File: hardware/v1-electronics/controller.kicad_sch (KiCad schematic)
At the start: 41 parts, among them IC1 IS31FL3733-QFLS4-TR, IC2 IS31FL3733-QFLS4-TR, IC3 IS31FL3741A-QFLS4-TR, U1 MDBT50Q-1MV2

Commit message: feat(v1 hardware): RGBW LED matrix halve 1
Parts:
- removed C27, C28, C29, C30, C31, C32, C34: C_Small, symbol Device:C_Small
- removed IC3: IS31FL3741A-QFLS4-TR, QFN40P700X700X80-61N-D, symbol Lumissil Microsystems:IS31FL3741A-QFLS4-TR
- removed R41, R42, R67: R_Small, symbol Device:R_Small
- added R148, R149, R150, R151, R152, R153, R154, R155, R156, R157, R158, R159, R160, R161, R162, R163, R164, R165, R166, R167, R168, R169, R170, R171, R172, R173, R174, R175, R176, R43, R44, R68: R_Small, symbol Device:R_Small
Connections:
- net GND: now also IC1.49 (EP), IC2.49 (EP)
- net I2C1_SCL: now also IC2.42 (SCL)
- net I2C1_SDA: now also IC2.41 (SDA); no longer IC2.45 (INTB), R115.2
- net SDB2: now also IC2.46 (SDB); no longer IC1.40 (SYNC), IC2.40 (SYNC)
- net ISET1 renamed R_EXT1
- net ISET2 renamed R_EXT2
- new net CS10_G_1: R163.1
- new net CS10_G_2: R164.1
- new net CS11_R_1: R165.1
- new net CS11_R_2: R166.1
- new net CS12_W_1: R167.1
- new net CS12_W_2: R168.1
- new net CS13_B_1: R169.1
- new net CS13_B_2: R170.1
- new net CS14_G_1: R171.1
- new net CS14_G_2: R172.1
- new net CS15_R_1: R173.1
- new net CS15_R_2: R174.1
- new net CS16_W_1: R175.1
- new net CS16_W_2: R176.1
- new net CS1_B_1: R43.1
- new net CS1_B_2: R148.1
- new net CS2_G_1: R44.1
- new net CS2_G_2: R149.1
- new net CS3_R_1: R68.1
- new net CS3_R_2: R150.1
- new net CS4_W_1: R151.1
- new net CS4_W_2: R152.1
- new net CS5_B_1: R153.1
- new net CS5_B_2: R154.1
- new net CS6_G_1: R155.1
- new net CS6_G_2: R156.1
- new net CS7_R_1: R157.1
- new net CS7_R_2: R158.1
- new net CS8_W_1: R159.1
- new net CS8_W_2: R160.1
- new net CS9_B_1: R161.1
- new net CS9_B_2: R162.1
- new net INTB2: IC2.45 (INTB), R115.2
- new net SYNC: IC1.40 (SYNC), IC2.40 (SYNC)
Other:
- note removed: "Some thought needs to be done as to what V_IO/MCU should be"
- moved on the sheet: C21, C22, C23, C24, C25, C26, C33, C35, C36, C37, C38, C39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

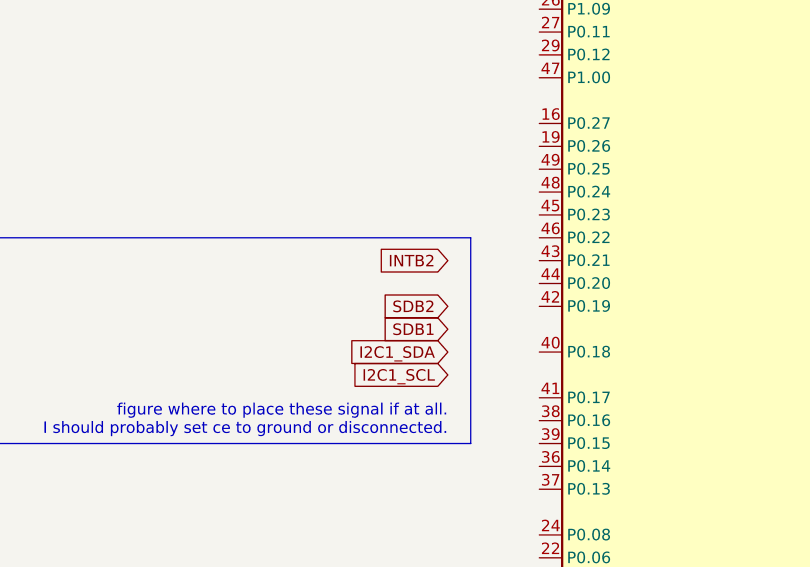
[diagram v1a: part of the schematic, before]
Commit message: feat(v1 hardware):second half of LED Matrix
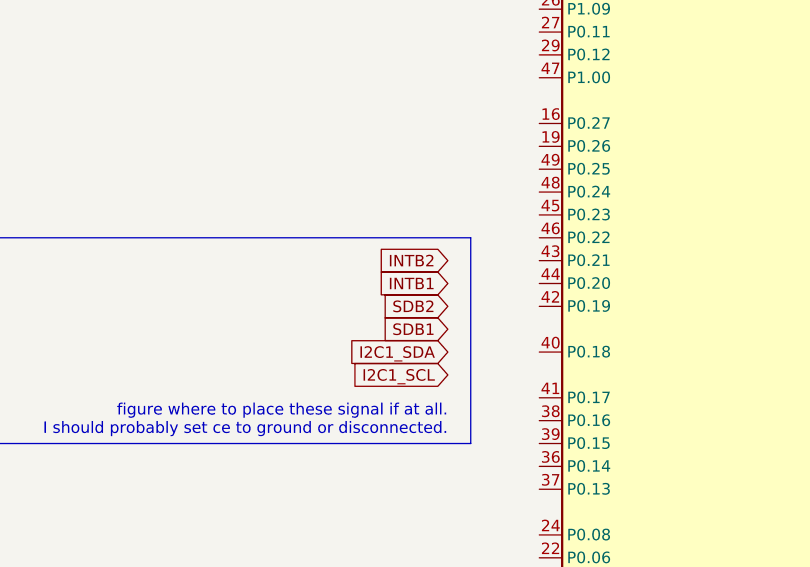
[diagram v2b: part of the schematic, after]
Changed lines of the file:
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@@
+		)
+	)
+	(global_label "INTB1"
+		(shape input)
+		(at 317.5 66.04 180)
+		(fields_autoplaced yes)
+		(effects
+			(font
+				(size 1.27 1.27)
+			)
+			(justify right)
+		)
+		(property "Intersheetrefs" "${INTERSHEET_REFS}"
+			(at 309.1324 66.04 0)
+			(hide yes)
+			(show_name no)
+			(do_not_autoplace no)
+			(effects
+				(font
+					(size 1.27 1.27)
+				)
+				(justify right)
+			)
 		)
 	)

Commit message: feat(v1 hardware): clean up led matrix
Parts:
- removed R148, R149, R150, R151, R152, R153, R154, R155, R156, R157, R158, R159, R160, R161, R162, R163, R164, R165, R166, R167, R168, R169, R170, R171, R172, R173, R174, R175, R176, R43, R44, R68: R_Small, symbol Device:R_Small
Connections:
- net CS10_G_1: now also IC1.26 (CS10)
- net CS10_G_2: now also IC2.26 (CS10)
- net CS11_R_1: now also IC1.27 (CS11)
- net CS11_R_2: now also IC2.27 (CS11)
- net CS12_W_1: now also IC1.28 (CS12)
- net CS12_W_2: now also IC2.28 (CS12)
- net CS13_B_1: now also IC1.30 (CS13)
- net CS13_B_2: now also IC2.30 (CS13)
- net CS14_G_1: now also IC1.31 (CS14)
- net CS14_G_2: now also IC2.31 (CS14)
- net CS15_R_1: now also IC1.32 (CS15)
- net CS15_R_2: now also IC2.32 (CS15)
- net CS16_W_1: now also IC1.33 (CS16)
- net CS16_W_2: now also IC2.33 (CS16)
- net CS1_B_1: now also IC1.16 (CS1)
- net CS1_B_2: now also IC2.16 (CS1)
- net CS2_G_1: now also IC1.17 (CS2)
- net CS2_G_2: now also IC2.17 (CS2)
- net CS3_R_1: now also IC1.18 (CS3)
- net CS3_R_2: now also IC2.18 (CS3)
- net CS4_W_1: now also IC1.19 (CS4)
- net CS4_W_2: now also IC2.19 (CS4)
- net CS5_B_1: now also IC1.21 (CS5)
- net CS5_B_2: now also IC2.21 (CS5)
- net CS6_G_1: now also IC1.22 (CS6)
- net CS6_G_2: now also IC2.22 (CS6)
- net CS7_R_1: now also IC1.23 (CS7)
- net CS7_R_2: now also IC2.23 (CS7)
- net CS8_W_1: now also IC1.24 (CS8)
- net CS8_W_2: now also IC2.24 (CS8)
- net CS9_B_1: now also IC1.25 (CS9)
- net CS9_B_2: now also IC2.25 (CS9)
- net SW10_1: now also IC1.13 (SW10)
- net SW10_2: now also IC2.13 (SW10)
- net SW11_1: now also IC1.14 (SW11)
- net SW11_2: now also IC2.14 (SW11)
- net SW12_1: now also IC1.15 (SW12)
- net SW12_2: now also IC2.15 (SW12)
- net SW1_1: now also IC1.2 (SW1)
- net SW1_2: now also IC2.2 (SW1)
- net SW2_1: now also IC1.3 (SW2)
- net SW2_2: now also IC2.3 (SW2)
- net SW3_1: now also IC1.4 (SW3)
- net SW3_2: now also IC2.4 (SW3)
- net SW4_1: now also IC1.6 (SW4)
- net SW4_2: now also IC2.6 (SW4)
- net SW5_1: now also IC1.7 (SW5)
- net SW5_2: now also IC2.7 (SW5)
- net SW6_1: now also IC1.8 (SW6)
- net SW6_2: now also IC2.8 (SW6)
- net SW7_1: now also IC1.9 (SW7)
- net SW7_2: now also IC2.9 (SW7)
- net SW8_1: now also IC1.10 (SW8)
- net SW8_2: now also IC2.10 (SW8)
- net SW9_1: now also IC1.11 (SW9)
- net SW9_2: now also IC2.11 (SW9)
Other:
- note added: "LED Matric IC 1"
- note added: "LED Matric IC 2"
- moved on the sheet: C24, C25, C26, C33, C35, C36, C37, C38, C39, C40, C41, C42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

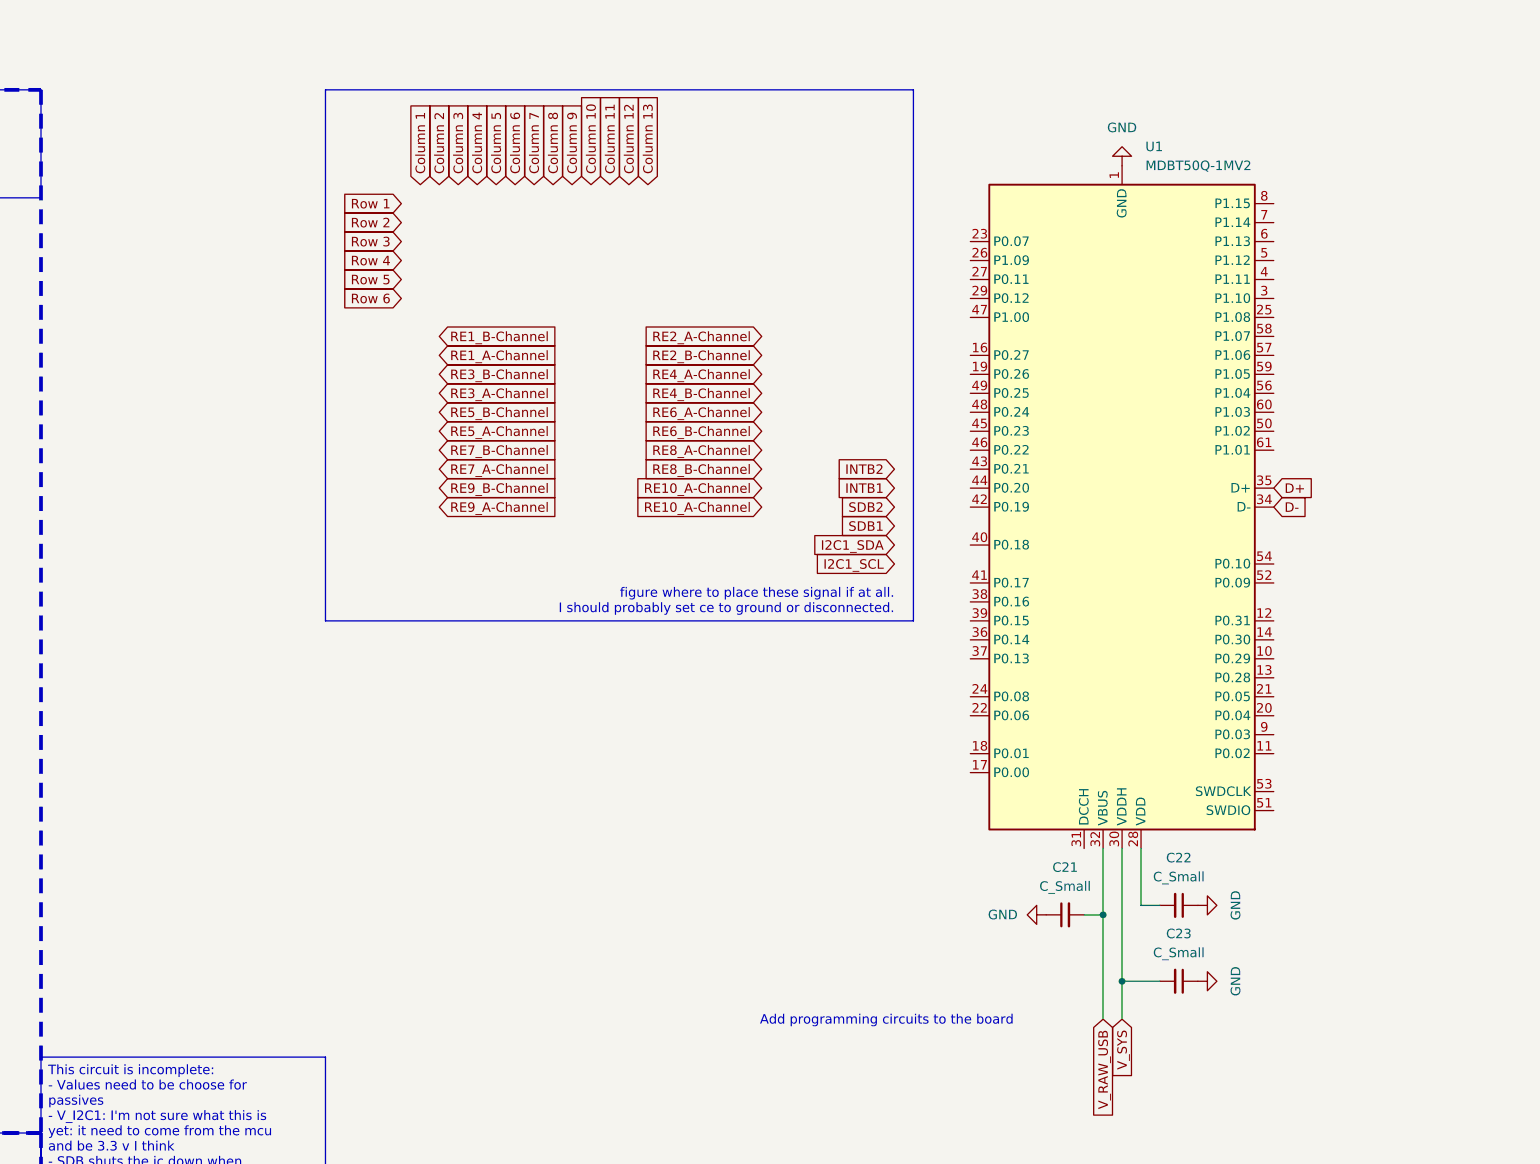
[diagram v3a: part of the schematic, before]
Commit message: feat(v1 hardware): start assigning pins on th mcu
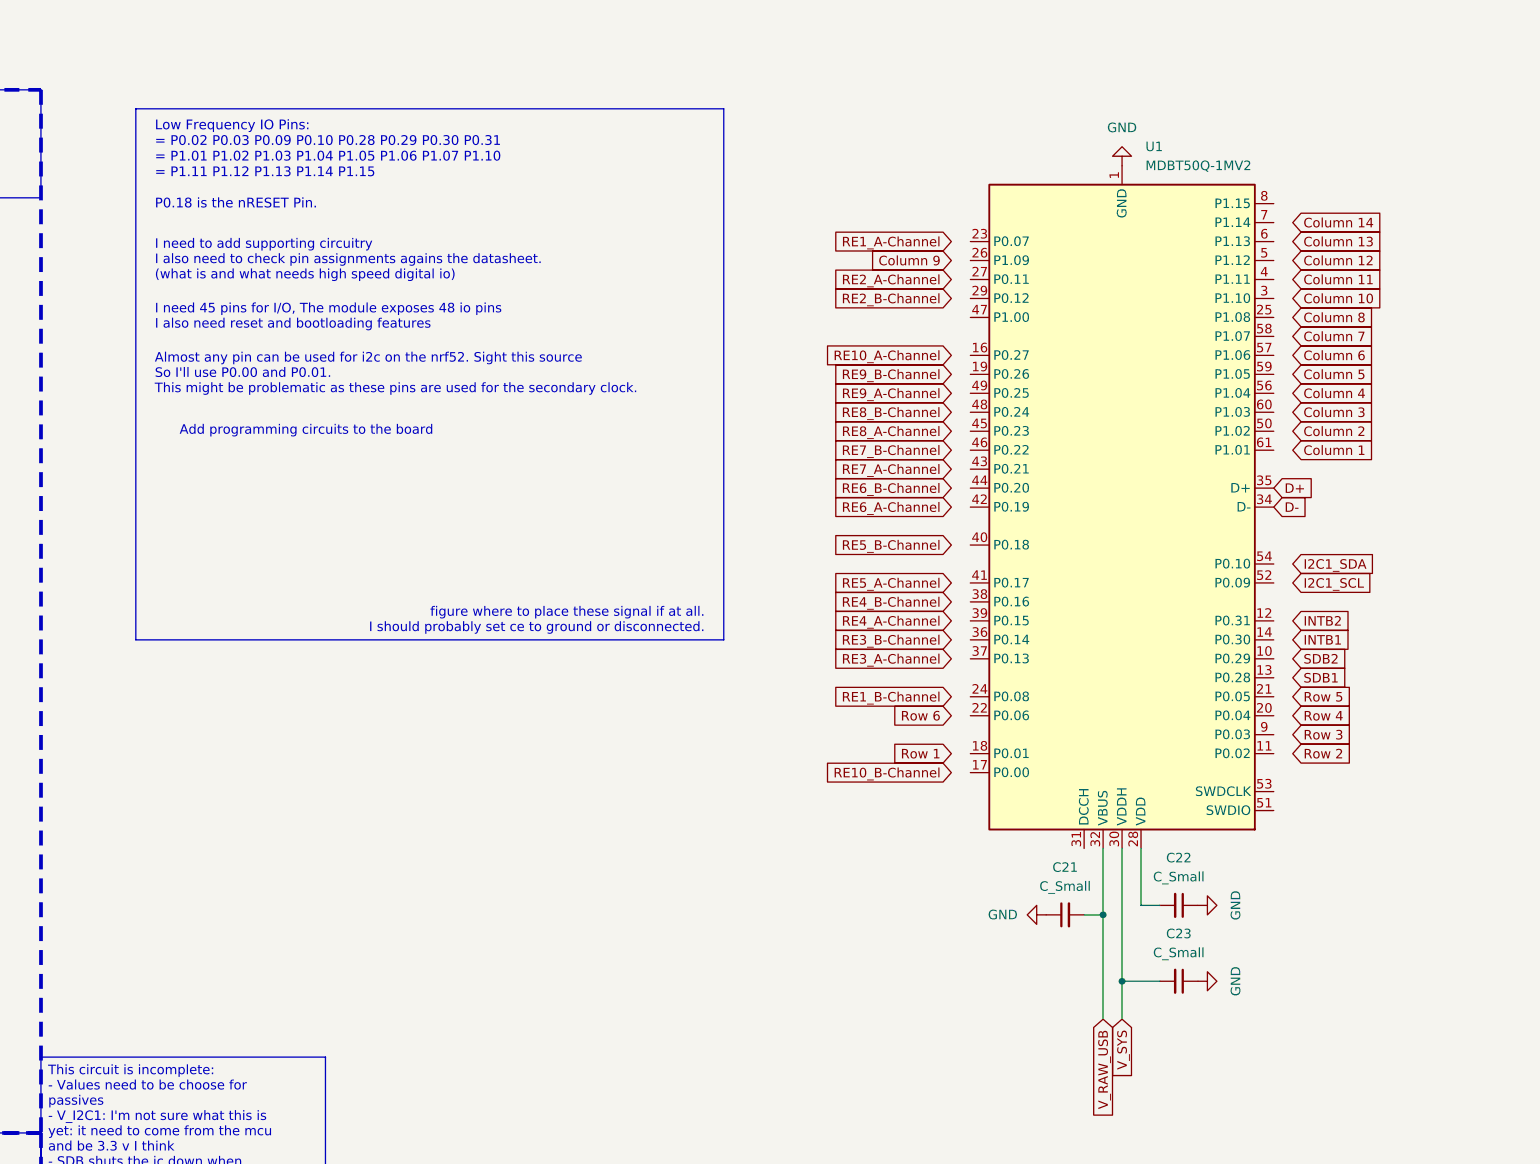
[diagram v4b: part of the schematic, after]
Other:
- note added: "Almost any pin can be used for i2c on the nrf52. Sight this source So I'll use P0.00 and P0.01. This might be problematic as these pins are used for the secondary clock."
- note added: "I need 45 pins for I/O, The module exposes 48 io pins I also need reset and bootloading features"
- note added: "I need to add supporting circuitry I also need to check pin assignments agains the datasheet. (what is and what needs high speed digital io)"
- note added: "Low Frequency IO Pins: = P0.02 P0.03 P0.09 P0.10 P0.28 P0.29 P0.30 P0.31 = P1.01 P1.02 P1.03 P1.04 P1.05 P1.06 P1.07 P1.10 = P1.11 P1.12 P1.13 P1.14 P1.15 P0.18 is the nRESET Pin."

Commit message: feat(v1 hardware): refine controller schematic
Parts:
- added J2: Conn_01x03, symbol Connector_Generic:Conn_01x03
- added R41, R42, R43, R44: R_Small, symbol Device:R_Small
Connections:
- net Column 1: now also U1.61 (P1.01)
- net Column 10: now also U1.3 (P1.10)
- net Column 11: now also U1.4 (P1.11)
- net Column 12: now also U1.5 (P1.12)
- net Column 13: now also U1.6 (P1.13)
- net Column 14: now also U1.7 (P1.14)
- net Column 2: now also U1.50 (P1.02)
- net Column 3: now also U1.60 (P1.03)
- net Column 4: now also U1.56 (P1.04)
- net Column 5: now also U1.59 (P1.05)
- net Column 6: now also U1.57 (P1.06)
- net Column 7: now also U1.58 (P1.07)
- net Column 8: now also U1.25 (P1.08)
- net Column 9: now also U1.26 (P1.09)
- net GND: now also C22.2, J2.2 (Pin_2); no longer C22.1
- net I2C1_SCL: now also U1.29 (P0.12), R42.2
- net I2C1_SDA: now also U1.27 (P0.11), R41.2
- net RE10_A-Channel: now also U1.13 (P0.28)
- net RE10_B-Channel: now also U1.10 (P0.29)
- net RE1_A-Channel: now also U1.23 (P0.07)
- net RE1_B-Channel: now also U1.24 (P0.08)
- net RE2_A-Channel: now also U1.52 (P0.09)
- net RE2_B-Channel: now also U1.54 (P0.10)
- net RE3_A-Channel: now also U1.37 (P0.13)
- net RE3_B-Channel: now also U1.36 (P0.14)
- net RE4_A-Channel: now also U1.39 (P0.15)
- net RE4_B-Channel: now also U1.38 (P0.16)
- net RE5_A-Channel: now also U1.41 (P0.17)
- net RE5_B-Channel: now also U1.42 (P0.19)
- net RE6_A-Channel: now also U1.44 (P0.20)
- net RE6_B-Channel: now also U1.43 (P0.21)
- net RE7_A-Channel: now also U1.46 (P0.22)
- net RE7_B-Channel: now also U1.45 (P0.23)
- net RE8_A-Channel: now also U1.48 (P0.24)
- net RE8_B-Channel: now also U1.49 (P0.25)
- net RE9_A-Channel: now also U1.19 (P0.26)
- net RE9_B-Channel: now also U1.16 (P0.27)
- net Row 1: now also U1.18 (P0.01)
- net Row 2: now also U1.11 (P0.02)
- net Row 3: now also U1.9 (P0.03)
- net Row 4: now also U1.20 (P0.04)
- net Row 5: now also U1.21 (P0.05)
- net Row 6: now also U1.22 (P0.06)
- net VDD: now reaches U1.28 (VDD)
- net VDD: now also C22.1, R41.1, R42.1; no longer C22.2
- net RESET: now reaches U1.40 (P0.18)
- net SWDIO: now reaches U1.51 (SWDIO)
- net SWDIO: now also R44.1
- net SWDCLK: now reaches U1.53 (SWDCLK)
- net SWDCLK: now also R43.1
- new net: J2.1 (Pin_1), R43.2
- new net: J2.3 (Pin_3), R44.2
- no-connect marks 4 -> 44
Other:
- note added: "Consider if there enough space for UART debug."
- note added: "I'll likily need to change to use a I2C charger."
- note added: "I'm uncertain about how to (if at all) decouple the VDD line"
- note added: "I2C Bus Config"
- note added: "Loose Notes"
- note added: "Low Frequency IO Pins: = P0.02 P0.03 P0.09 P0.10 P0.28 P0.29 P0.30 P0.31 = P1.01 P1.02 P1.03 P1.04 P1.05 P1.06 P1.07 P1.10 = P1.11 P1.12 P1.13 P1.14 P1.15 Standard Frequency IO Pins: = P0.00 P0.01 P0.04 P0.05 P0.06 P0.07 P0.08 P0.11 = P0.12 P0.13 P0.14 P0.15 P0.16 P0.17 P0.18 P0.19 = P0.20 P0.21 P0.22 P0.23 P0.24 P0.25 P0.26 P0.27 = P1.00 P1.08 P1.09 P0.18 is the nRESET Pin."
- note added: "Microcontroller"
- note added: "Power Config"
- note added: "Programmer"
- note added: "Rotary Encoders"
- note added: "Set up resets for the device."
- note added: "Switch Matrix"
- note added: "USB Config"
- note added: "Unassigned Pins"
- note removed: "Add programming circuits to the board"
- note removed: "Low Frequency IO Pins: = P0.02 P0.03 P0.09 P0.10 P0.28 P0.29 P0.30 P0.31 = P1.01 P1.02 P1.03 P1.04 P1.05 P1.06 P1.07 P1.10 = P1.11 P1.12 P1.13 P1.14 P1.15 P0.18 is the nRESET Pin."
- moved on the sheet: C21, U1
